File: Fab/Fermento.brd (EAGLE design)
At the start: 85 x 68 mm, 30 parts, among them Q1 32.768kHz, Q2 P-MOSFET

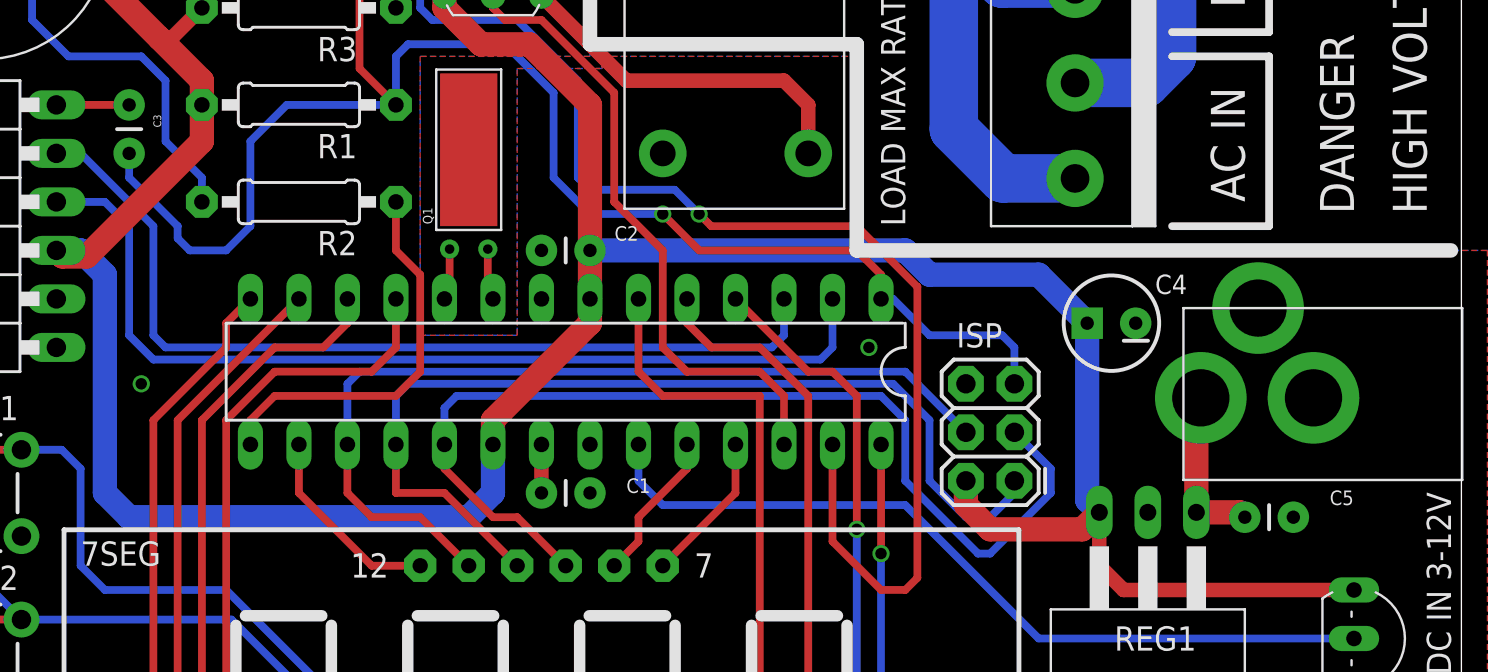
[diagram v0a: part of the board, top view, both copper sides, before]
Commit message: Added kindof datasheet for Fab board.
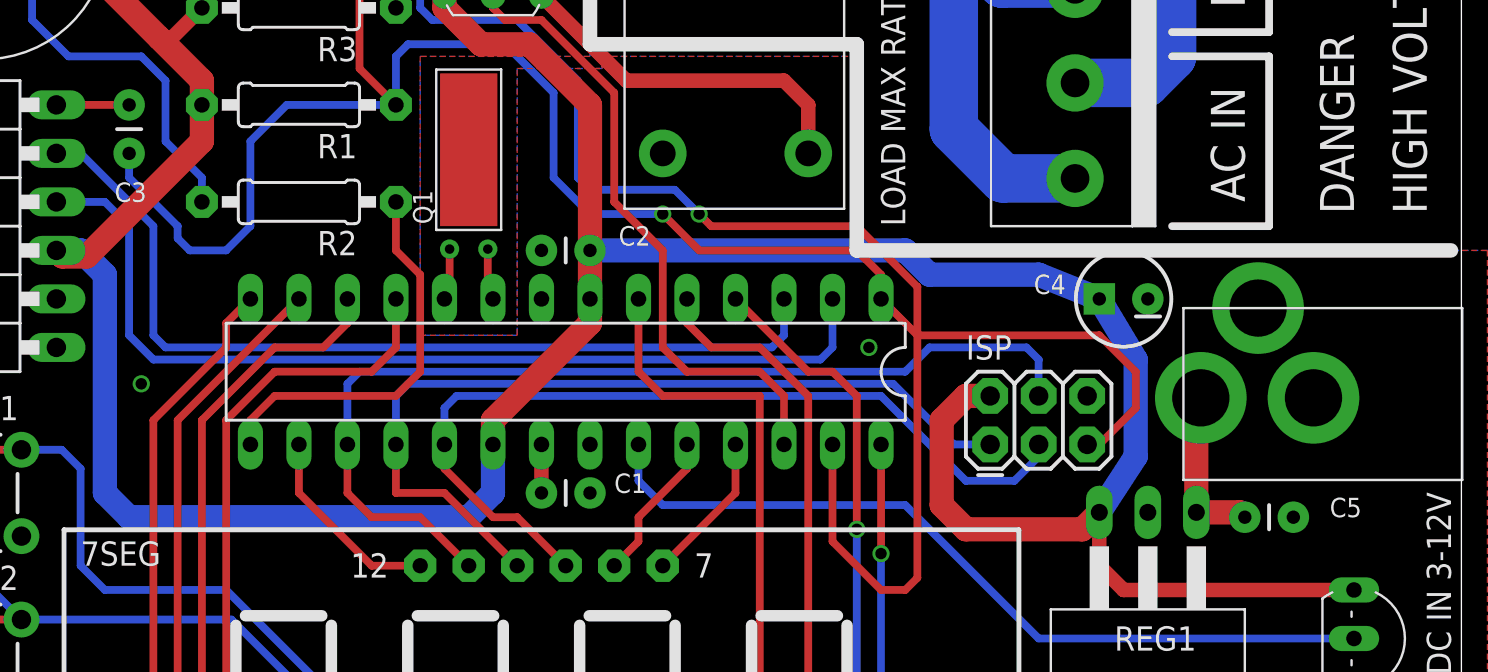
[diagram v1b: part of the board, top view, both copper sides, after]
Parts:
- moved ISP 2.29 mm to (60.3, 25.4), turned to 0 degrees
- moved C4 1.42 mm to (67.3, 33.0)
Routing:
- net RESET: track 92.4 -> 102.7 mm
- net VCC: track 171.6 -> 181.0 mm
- net DIG2: track 54.2 -> 46.0 mm
- net F: track 51.6 -> 45.7 mm
- net A: track 47.6 -> 52.8 mm
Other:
- board text added: "Mount screws: M3"
